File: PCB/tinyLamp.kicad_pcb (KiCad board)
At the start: 2 copper layers, 50 x 38 mm, 53 parts, among them J11 USB_B_Mini, J12 Conn_02x03_Odd_Even, Q21 Q_NPN_BCE, Q22 Q_NPN_BCE, Q23 Q_NPN_BCE, Q31 Q_NPN_BCE, Q41 Q_NPN_BCE, SW11 SW_Push, SW12 SW_Push, SW13 SW_Push, U11 TP4056, U12 ATtiny24A-SS, X11 BATT+, X12 BATT-

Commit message: made some changes
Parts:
- removed C11: 1nF, Capacitor_SMD:C_1206_3216Metric_Pad1.33x1.80mm_HandSolder
- removed D33, D34, D35, D36, D37, D38: LEDA, LED_SMD:LED_0805_2012Metric_Pad1.15x1.40mm_HandSolder
- removed D41, D42, D43, D44: LEDW, LED_SMD:LED_PLCC-2
- removed Q21, Q22, Q23, Q31, Q41: Q_NPN_BCE, Package_TO_SOT_SMD:SOT-23
- removed R16: 2k, Resistor_SMD:R_1206_3216Metric_Pad1.30x1.75mm_HandSolder
- removed R17, R18: 1K, Resistor_SMD:R_1206_3216Metric_Pad1.30x1.75mm_HandSolder
- removed R21, R22, R23, R31, R32: 110R, Resistor_SMD:R_1206_3216Metric_Pad1.30x1.75mm_HandSolder
- removed R41, R42: 15R, Resistor_SMD:R_1206_3216Metric_Pad1.30x1.75mm_HandSolder
- removed SW11, SW12, SW13: SW_Push, Button_Switch_SMD:SW_SPST_CK_RS282G05A3
- removed U12: ATtiny24A-SS, Package_SO:SOIC-14_3.9x8.7mm_P1.27mm
- removed X11: BATT+, TestPoint:TestPoint_Keystone_5015_Micro-Minature
- removed X12: BATT-, TestPoint:TestPoint_Keystone_5015_Micro-Minature
- added D14: LED_W, LED_THT:LED_D3.0mm_FlatTop, F.Cu at (34.5, 16.0)
- added D15: LED_W, LED_THT:LED_D3.0mm_FlatTop, F.Cu at (29.5, 24.5)
- added D16: LED_W, LED_THT:LED_D3.0mm_FlatTop, F.Cu at (29.5, 19.0)
- added D17: LED_W, LED_THT:LED_D3.0mm_FlatTop, F.Cu at (39.5, 24.5)
- added D18: LED_W, LED_THT:LED_D3.0mm_FlatTop, F.Cu at (39.5, 19.0)
- added D19: LED_O, LED_THT:LED_D3.0mm_FlatTop, F.Cu at (29.5, 10.5)
- added D20: LED_O, LED_THT:LED_D3.0mm_FlatTop, F.Cu at (29.5, 16.0)
- added D29: WS2812B, LED_SMD:LED_WS2812B_PLCC4_5.0x5.0mm_P3.2mm, F.Cu at (89.0, 11.5)
- added D30: WS2812B, LED_SMD:LED_WS2812B_PLCC4_5.0x5.0mm_P3.2mm, F.Cu at (89.0, 20.5)
- added Q11: BC547, Package_TO_SOT_THT:TO-92L_HandSolder, F.Cu at (66.2, -22.2)
- added Q12: BC547, Package_TO_SOT_THT:TO-92L_HandSolder, F.Cu at (66.2, -16.1)
- D11: value D -> LED_W; footprint Diode_SMD:D_SOD-123 -> LED_THT:LED_D3.0mm_FlatTop; moved to F.Cu
- D12: value LEDG -> LED_W; footprint LED_SMD:LED_0805_2012Metric_Pad1.15x1.40mm_HandSolder -> LED_THT:LED_D3.0mm_FlatTop
- D13: value LEDA -> LED_W; footprint LED_SMD:LED_0805_2012Metric_Pad1.15x1.40mm_HandSolder -> LED_THT:LED_D3.0mm_FlatTop
- D21, D22, D23, D24, D25, D26: value LED_RGB -> LED_O; footprint LED_SMD:LED_RGB_5050-6 -> LED_THT:LED_D3.0mm_FlatTop
- D27, D28: value LED_RGB -> WS2812B; footprint LED_SMD:LED_RGB_5050-6 -> LED_SMD:LED_WS2812B_PLCC4_5.0x5.0mm_P3.2mm
- D31, D32: value LEDA -> WS2812B; footprint LED_SMD:LED_0805_2012Metric_Pad1.15x1.40mm_HandSolder -> LED_SMD:LED_WS2812B_PLCC4_5.0x5.0mm_P3.2mm
- J11: value USB_B_Mini -> Conn_01x02_Pin; footprint Connector_USB:USB_Mini-B_Lumberg_2486_01_Horizontal -> Connector_PinHeader_2.54mm:PinHeader_1x02_P2.54mm_Vertical; moved to F.Cu
- J12: value Conn_02x03_Odd_Even -> Conn_01x02_Pin; footprint Connector_PinHeader_2.54mm:PinHeader_2x03_P2.54mm_Vertical -> Connector_PinHeader_2.54mm:PinHeader_1x02_P2.54mm_Vertical
- R11, R12, R13: value 1K -> 110R; footprint Resistor_SMD:R_1206_3216Metric_Pad1.30x1.75mm_HandSolder -> Resistor_THT:R_Axial_DIN0207_L6.3mm_D2.5mm_P10.16mm_Horizontal
- R14, R15: value 1k -> 110R; footprint Resistor_SMD:R_1206_3216Metric_Pad1.30x1.75mm_HandSolder -> Resistor_THT:R_Axial_DIN0207_L6.3mm_D2.5mm_P10.16mm_Horizontal
- U11: value TP4056 -> WeMos_D1_mini; footprint Package_SO:HSOP-8-1EP_3.9x4.9mm_P1.27mm_EP2.3x2.3mm -> Module:WEMOS_D1_mini_light; moved to B.Cu
- moved U11 98.5 mm to (93.9, 8.61), turned to 180 degrees
- moved D31 92.2 mm to (83.0, 20.5)
- moved D32 84.4 mm to (77.0, 20.5)
- moved J12 82.9 mm to (65.3, -7.04), turned to 0 degrees
- moved J11 79.8 mm to (60.6, -7.04), turned to 0 degrees
- moved R14 74.8 mm to (61.3, -11.0), turned to 0 degrees
- moved R12 68.8 mm to (61.3, -20.9)
- moved D28 63.2 mm to (83.0, 11.5)
- moved R11 62.3 mm to (47.9, -24.5)
- moved R13 62.0 mm to (61.3, -14.3)
- moved R15 61.9 mm to (61.3, -17.6), turned to 0 degrees
- moved D21 61.7 mm to (39.5, 10.5), turned to 90 degrees
- moved D22 61.1 mm to (39.5, 16.0), turned to 90 degrees
- moved D27 55.9 mm to (77.0, 11.5)
- moved D24 51.0 mm to (24.5, 19.0)
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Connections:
- D11 pad 1: /EXTOUT -> Net-(D11-K)
- D11 pad 2: VCC -> +5V
- D12 pad 1: Net-(D12-Pad1) -> Net-(D12-K)
- D12 pad 2: Net-(D12-Pad2) -> Net-(D11-K)
- D13 pad 1: Net-(D13-Pad1) -> Net-(D13-K)
- D13 pad 2: Net-(D12-Pad2) -> +5V
- D21 pad 1: /RGBleds/Rch -> Net-(D21-K)
- D21 pad 2: /RGBleds/Gch -> +5V
- D22 pad 1: /RGBleds/Rch -> Net-(D20-K)
- D22 pad 2: /RGBleds/Gch -> Net-(D21-K)
- D23 pad 1: /RGBleds/Rch -> Net-(D23-K)
- D23 pad 2: /RGBleds/Gch -> +5V
- D24 pad 1: /RGBleds/Rch -> Net-(D20-K)
- D24 pad 2: /RGBleds/Gch -> Net-(D23-K)
- D25 pad 1: /RGBleds/Rch -> Net-(D25-K)
- D25 pad 2: /RGBleds/Gch -> +5V
- D26 pad 1: /RGBleds/Rch -> Net-(D20-K)
- D26 pad 2: /RGBleds/Gch -> Net-(D25-K)
- D27 pad 1: /RGBleds/Rch -> +5V
- D27 pad 2: /RGBleds/Gch -> Net-(D27-DOUT)
- D27 pad 3: /RGBleds/Bch -> GND
- D27 pad 4: VCC -> Net-(D27-DIN)
- D28 pad 1: /RGBleds/Rch -> +5V
- D28 pad 2: /RGBleds/Gch -> Net-(D28-DOUT)
- D28 pad 3: /RGBleds/Bch -> GND
- D28 pad 4: VCC -> Net-(D27-DOUT)
- D31 pad 1: Net-(D31-Pad1) -> +5V
- D31 pad 2: VCC -> Net-(D31-DOUT)
- D32 pad 1: Net-(D31-Pad1) -> +5V
- D32 pad 2: VCC -> unconnected-(D32-DOUT-Pad2)
- J11 pad 1: VBUS -> +5V
- J11 pad 2: Net-(J11-Pad2) -> GND
- J12 pad 1: /MISO_PWM3 -> +5V
- J12 pad 2: VBUS -> GND
- R11 pad 1: /PWM1 -> Net-(Q11-B)
- R11 pad 2: /RGBleds/LEDG -> /LEDW
- R12 pad 1: /PWM0 -> Net-(Q11-C)
- R12 pad 2: /RGBleds/LEDR -> Net-(D12-K)
- R13 pad 1: /MOSI_PWM2 -> Net-(Q12-B)
- R13 pad 2: /LEDR_EN -> /LEDO
- R14 pad 1: Net-(J11-Pad2) -> Net-(Q12-C)
- R14 pad 2: /INT3_DATA -> Net-(D20-K)
- R15 pad 1: Net-(D12-Pad2) -> Net-(D27-DIN)
- R15 pad 2: VBUS -> /LEDA
- U11 pad 1: GND -> unconnected-(U11-~{RST}-Pad1)
- U11 pad 2: /PROG -> unconnected-(U11-A0-Pad2)
- U11 pad 3: GND -> unconnected-(U11-D0-Pad3)
- U11 pad 4: VBUS -> /LEDA
- U11 pad 5: VCC -> /LEDO
- U11 pad 6: Net-(D12-Pad1) -> /LEDW
- U11 pad 7: Net-(D13-Pad1) -> unconnected-(U11-CS/D8-Pad7)
- U11 pad 8: VBUS -> +3.3V
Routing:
- net VCC: track 192.5 -> 0.00 mm, vias 2 -> 0
- net /RGBleds/Bch: track 128.9 -> 0.00 mm, vias 8 -> 0
- net /RGBleds/Gch: track 124.8 -> 0.00 mm, vias 8 -> 0
- net /RGBleds/Rch: track 120.3 -> 0.00 mm, vias 8 -> 0
- net /MISO_PWM3: track 57.8 -> 0.00 mm, vias 1 -> 0
- net VBUS: track 50.1 -> 0.00 mm, vias 3 -> 0
- net /INT3_DATA: track 35.6 -> 0.00 mm
- net /MOSI_PWM2: track 33.4 -> 0.00 mm, vias 2 -> 0
- net Net-(Q41-Pad2): track 31.3 -> 0.00 mm
- net /SW_M: track 24.8 -> 0.00 mm, vias 2 -> 0
- net /LEDA_EN: track 24.4 -> 0.00 mm, vias 2 -> 0
- net /SW_P: track 18.3 -> 0.00 mm
- net /LEDR_EN: track 17.8 -> 0.00 mm
- net /PWM0: track 15.8 -> 0.00 mm
- net /PWM1: track 15.1 -> 0.00 mm, vias 2 -> 0
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- removed copper zone on B.Cu, net GND
- removed copper zone on F.Cu, net GND
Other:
- board size 50 x 38 mm -> 96 x 34.7 mm
- board text removed: "1"
- board text removed: "2"
- board text removed: "3"
- board text removed: "4"
- board text removed: "5"
- board text removed: "6"
- board text removed: "Jonah Wille"
- board text removed: "tinyLamp"

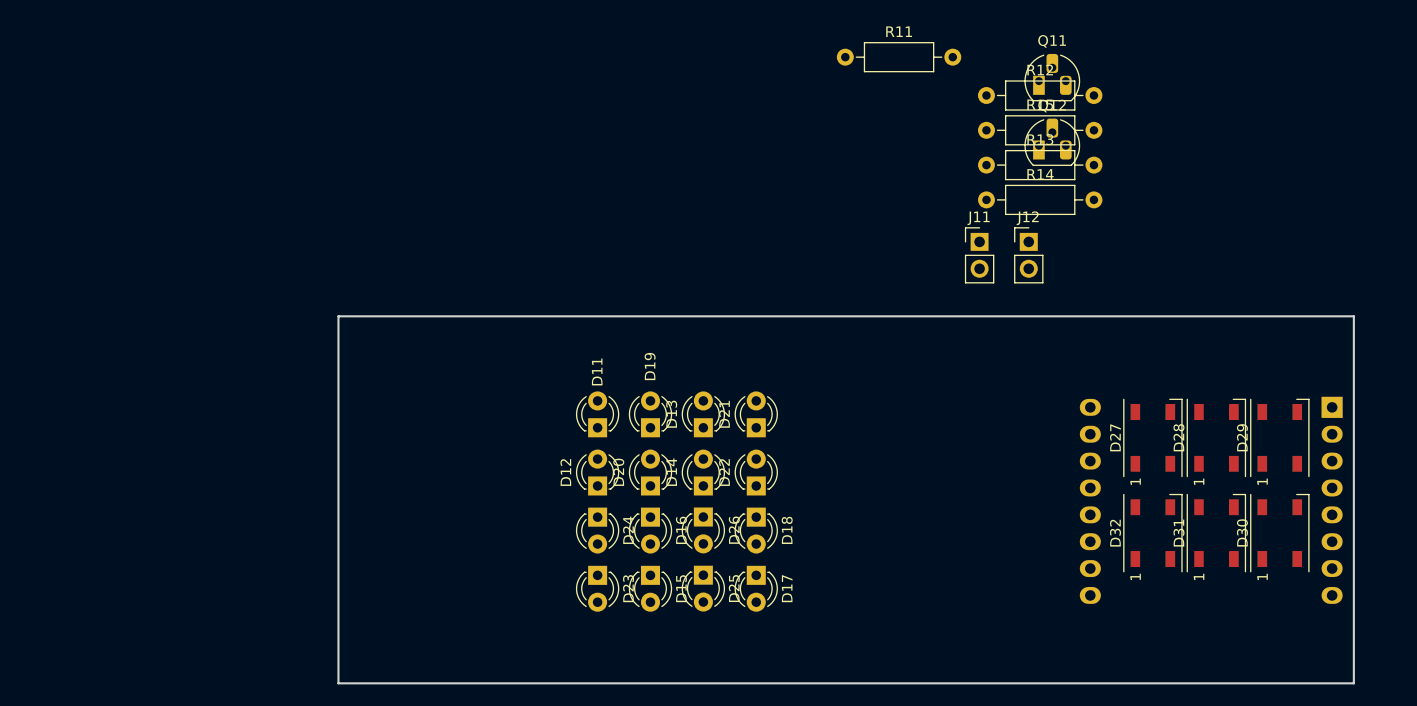
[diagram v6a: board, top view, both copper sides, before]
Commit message: pcb: placed leds
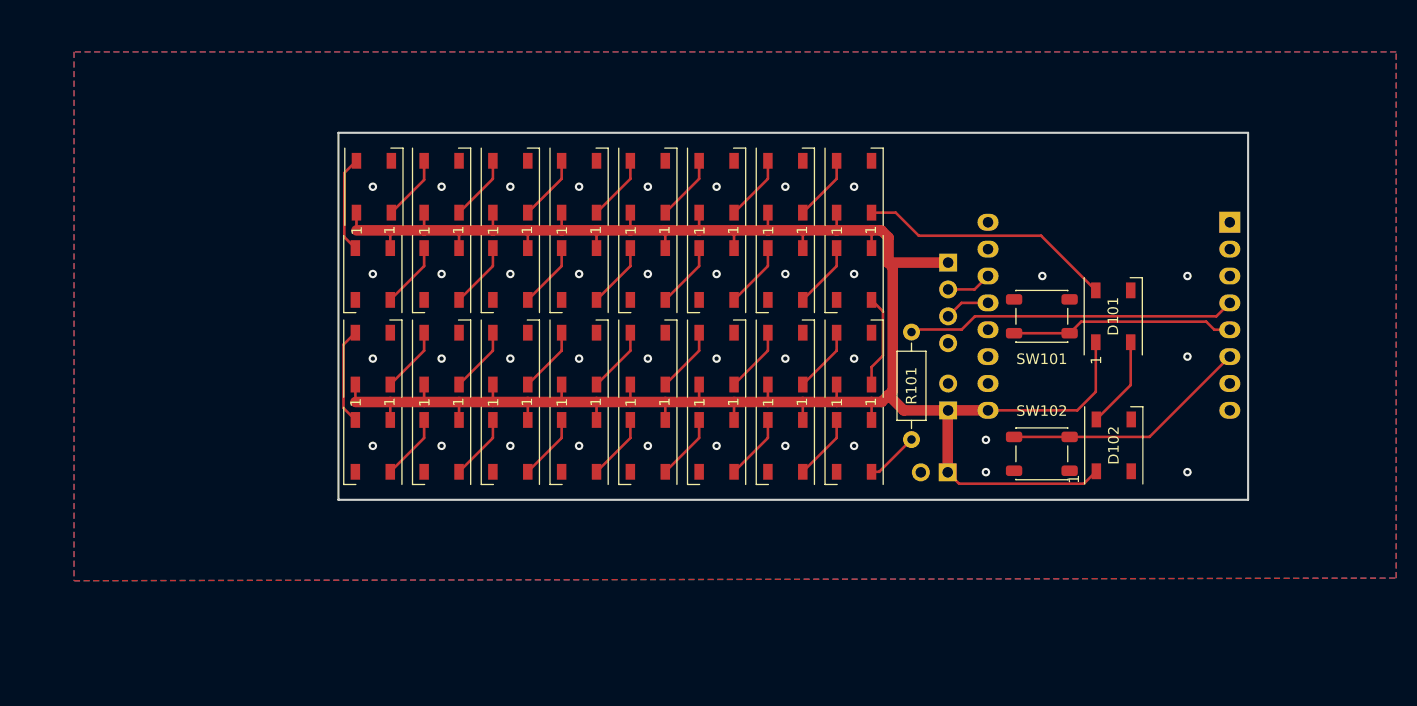
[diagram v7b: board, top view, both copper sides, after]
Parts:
- removed D11, D12, D13, D14, D15, D16, D17, D18: LED_W, LED_THT:LED_D3.0mm_FlatTop
- removed D19, D20, D21, D22, D23, D24, D25, D26: LED_O, LED_THT:LED_D3.0mm_FlatTop
- removed D27, D28, D29, D30, D31, D32: WS2812B, LED_SMD:LED_WS2812B_PLCC4_5.0x5.0mm_P3.2mm
- removed Q11, Q12: BC547, Package_TO_SOT_THT:TO-92L_HandSolder
- removed R11, R12, R13, R14, R15: 110R, Resistor_THT:R_Axial_DIN0207_L6.3mm_D2.5mm_P10.16mm_Horizontal
- added D101: WS2812B, LED_SMD:LED_WS2812B_PLCC4_5.0x5.0mm_P3.2mm, F.Cu at (73.2, 0.00)
- added D102: WS2812B, LED_SMD:LED_WS2812B_PLCC4_5.0x5.0mm_P3.2mm, F.Cu at (73.3, 12.2)
- added D201: WS2812B, LED_SMD:LED_WS2812B_PLCC4_5.0x5.0mm_P3.2mm, F.Cu at (48.8, 12.2)
- added D202: WS2812B, LED_SMD:LED_WS2812B_PLCC4_5.0x5.0mm_P3.2mm, F.Cu at (42.2, 12.2)
- added D203: WS2812B, LED_SMD:LED_WS2812B_PLCC4_5.0x5.0mm_P3.2mm, F.Cu at (35.8, 12.2)
- added D204: WS2812B, LED_SMD:LED_WS2812B_PLCC4_5.0x5.0mm_P3.2mm, F.Cu at (29.2, 12.2)
- added D205: WS2812B, LED_SMD:LED_WS2812B_PLCC4_5.0x5.0mm_P3.2mm, F.Cu at (22.8, 12.2)
- added D206: WS2812B, LED_SMD:LED_WS2812B_PLCC4_5.0x5.0mm_P3.2mm, F.Cu at (16.2, 12.2)
- added D207: WS2812B, LED_SMD:LED_WS2812B_PLCC4_5.0x5.0mm_P3.2mm, F.Cu at (9.75, 12.2)
- added D208: WS2812B, LED_SMD:LED_WS2812B_PLCC4_5.0x5.0mm_P3.2mm, F.Cu at (3.25, 12.2)
- added D209: WS2812B, LED_SMD:LED_WS2812B_PLCC4_5.0x5.0mm_P3.2mm, F.Cu at (3.25, 4.00)
- added D210: WS2812B, LED_SMD:LED_WS2812B_PLCC4_5.0x5.0mm_P3.2mm, F.Cu at (9.75, 4.00)
- added D211: WS2812B, LED_SMD:LED_WS2812B_PLCC4_5.0x5.0mm_P3.2mm, F.Cu at (16.2, 4.00)
- added D212: WS2812B, LED_SMD:LED_WS2812B_PLCC4_5.0x5.0mm_P3.2mm, F.Cu at (22.8, 4.00)
- added D213: WS2812B, LED_SMD:LED_WS2812B_PLCC4_5.0x5.0mm_P3.2mm, F.Cu at (29.2, 4.00)
- added D214: WS2812B, LED_SMD:LED_WS2812B_PLCC4_5.0x5.0mm_P3.2mm, F.Cu at (35.8, 4.00)
- added D215: WS2812B, LED_SMD:LED_WS2812B_PLCC4_5.0x5.0mm_P3.2mm, F.Cu at (42.2, 4.00)
- added D216: WS2812B, LED_SMD:LED_WS2812B_PLCC4_5.0x5.0mm_P3.2mm, F.Cu at (48.8, 4.00)
- added D217: WS2812B, LED_SMD:LED_WS2812B_PLCC4_5.0x5.0mm_P3.2mm, F.Cu at (48.8, -4.00)
- added D218: WS2812B, LED_SMD:LED_WS2812B_PLCC4_5.0x5.0mm_P3.2mm, F.Cu at (42.2, -4.00)
- added D219: WS2812B, LED_SMD:LED_WS2812B_PLCC4_5.0x5.0mm_P3.2mm, F.Cu at (35.8, -4.00)
- added D220: WS2812B, LED_SMD:LED_WS2812B_PLCC4_5.0x5.0mm_P3.2mm, F.Cu at (29.2, -4.00)
- added D221: WS2812B, LED_SMD:LED_WS2812B_PLCC4_5.0x5.0mm_P3.2mm, F.Cu at (22.8, -4.00)
- added D222: WS2812B, LED_SMD:LED_WS2812B_PLCC4_5.0x5.0mm_P3.2mm, F.Cu at (16.2, -4.00)
- added D223: WS2812B, LED_SMD:LED_WS2812B_PLCC4_5.0x5.0mm_P3.2mm, F.Cu at (9.75, -4.00)
- added D224: WS2812B, LED_SMD:LED_WS2812B_PLCC4_5.0x5.0mm_P3.2mm, F.Cu at (3.25, -4.00)
- added D225: WS2812B, LED_SMD:LED_WS2812B_PLCC4_5.0x5.0mm_P3.2mm, F.Cu at (3.35, -12.2)
- added D226: WS2812B, LED_SMD:LED_WS2812B_PLCC4_5.0x5.0mm_P3.2mm, F.Cu at (9.75, -12.2)
- added D227: WS2812B, LED_SMD:LED_WS2812B_PLCC4_5.0x5.0mm_P3.2mm, F.Cu at (16.2, -12.2)
- added D228: WS2812B, LED_SMD:LED_WS2812B_PLCC4_5.0x5.0mm_P3.2mm, F.Cu at (22.8, -12.2)
- added D229: WS2812B, LED_SMD:LED_WS2812B_PLCC4_5.0x5.0mm_P3.2mm, F.Cu at (29.2, -12.2)
- added D230: WS2812B, LED_SMD:LED_WS2812B_PLCC4_5.0x5.0mm_P3.2mm, F.Cu at (35.8, -12.2)
- added D231: WS2812B, LED_SMD:LED_WS2812B_PLCC4_5.0x5.0mm_P3.2mm, F.Cu at (42.2, -12.2)
- added D232: WS2812B, LED_SMD:LED_WS2812B_PLCC4_5.0x5.0mm_P3.2mm, F.Cu at (48.8, -12.2)
- added J103: Conn_01x04, Connector_PinHeader_2.54mm:PinHeader_1x04_P2.54mm_Vertical, B.Cu at (57.6, -5.08)
- added R101: 110R, Resistor_THT:R_Axial_DIN0207_L6.3mm_D2.5mm_P10.16mm_Horizontal, F.Cu at (54.2, 11.7)
- added SW101: SW_Push, Button_Switch_SMD:SW_SPST_PTS647_Sx50, F.Cu at (66.5, 0.00)
- added SW102: SW_Push, Button_Switch_SMD:SW_SPST_PTS647_Sx50, F.Cu at (66.5, 13.0)
- J101: renamed from J11; moved to B.Cu
- J102: renamed from J12; moved to B.Cu
- moved J102 23.1 mm to (57.6, 14.8), turned to 90 degrees
- moved U101 20.0 mm to (84.3, -8.89)
- moved J101 16.2 mm to (57.6, 8.89)
- renumbered U11 to U101
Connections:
- U101 pad 13: unconnected-(U11-SDA/D2-Pad13) -> /SDA
- U101 pad 14: unconnected-(U11-SCL/D1-Pad14) -> /SCL
- U101 pad 5: /LEDO -> /B1
- U101 pad 6: /LEDW -> /B2
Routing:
- net +5V: track 0.00 -> 222.2 mm
- net /LEDA: track 0.00 -> 31.2 mm
- net /leds/dataOut: track 0.00 -> 24.2 mm
- net /B2: track 0.00 -> 23.5 mm
- net /B1: track 0.00 -> 21.2 mm
- net Net-(D208-DOUT): track 0.00 -> 9.18 mm
- net Net-(D224-DOUT): track 0.00 -> 9.16 mm
- net Net-(D216-DOUT): track 0.00 -> 8.89 mm
- net Net-(D101-DOUT): track 0.00 -> 8.65 mm
- net Net-(D221-DOUT): track 0.00 -> 6.23 mm
- net Net-(D220-DOUT): track 0.00 -> 6.23 mm
- net Net-(D219-DOUT): track 0.00 -> 6.23 mm
- net Net-(D218-DOUT): track 0.00 -> 6.23 mm
- net Net-(D217-DOUT): track 0.00 -> 6.23 mm
- net Net-(D215-DOUT): track 0.00 -> 6.23 mm
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- added copper zone on B.Cu, net GND
- added copper zone on F.Cu, net GND
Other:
- board size 96 x 34.7 mm -> 86 x 34.7 mm
